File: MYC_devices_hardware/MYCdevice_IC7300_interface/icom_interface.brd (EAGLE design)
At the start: 83.8 x 32.7 mm, 42 parts, among them IC1 ATMEGA1284, IC2 MAX232, IC3 PCA9517, IC4 78L05, Q1 20MHz, Q2 BC817-40SMD, Q3 BC817-40SMD, Q4 BSS138, X1 8-15V, X2 1503_09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

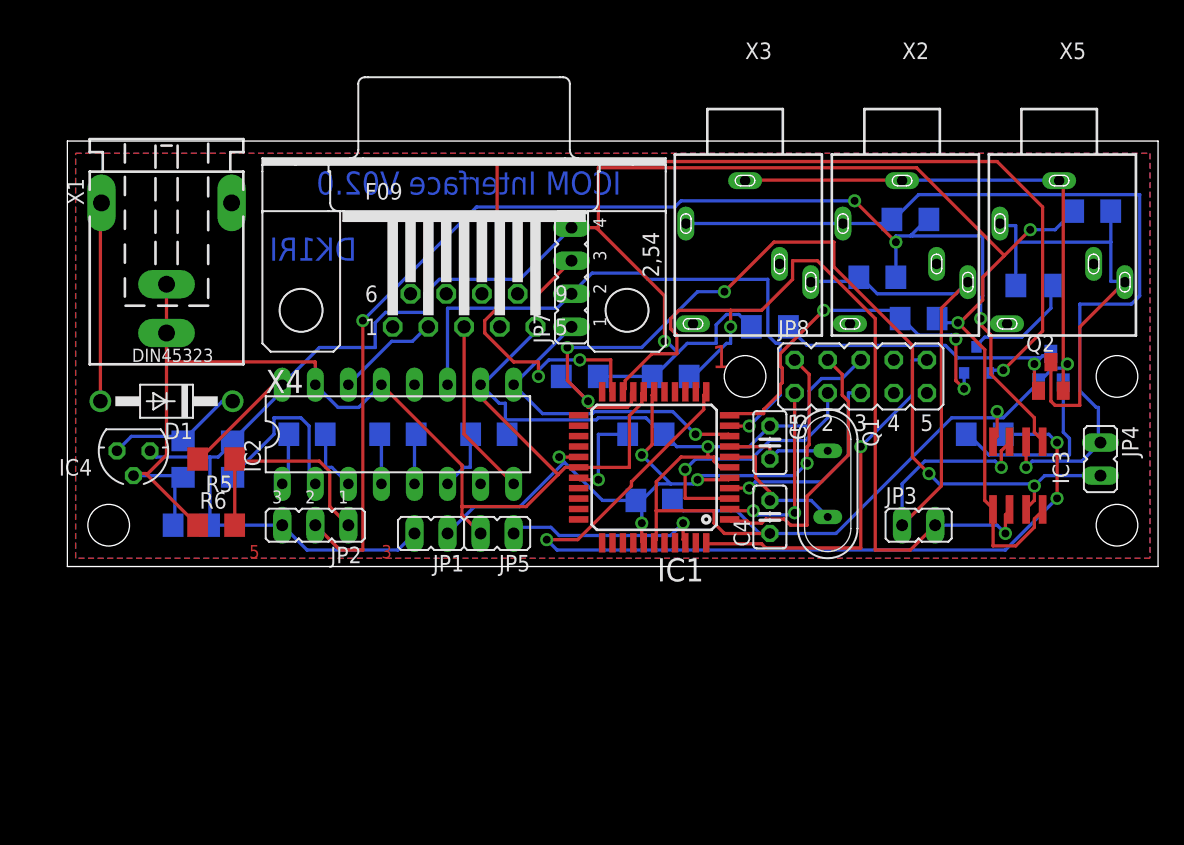
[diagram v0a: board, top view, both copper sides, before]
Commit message: wrong FET corrected, better layout
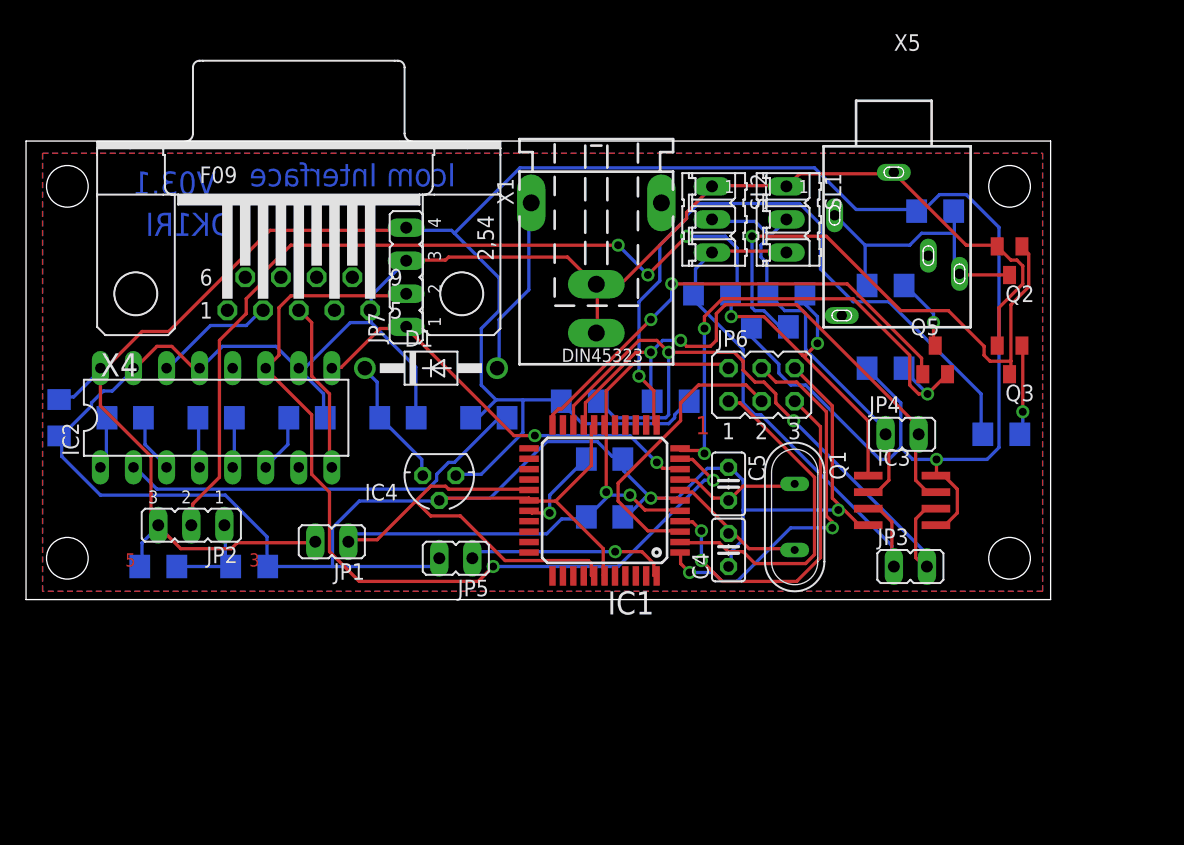
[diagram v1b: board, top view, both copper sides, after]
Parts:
- removed JP8: SPI/ISP, jumper:JP5Q
- removed Q4: BSS138, bss138_10:SOT23
- removed X2, X3: 1503_09, con-lumberg:1503_09
- added JP6: ISP, jumper:JP3Q
- added Q5: BSS84, transistor-small-signal:SOT23
- added SL1, SL2: I2C, con-amp-quick:03P
- C3: value 22uF 1210 -> 22uF
- R1, R2, R3, R4: value 10k -> see manual
- R10: value 100k -> 10k
- moved X1 33.0 mm to (43.8, 45.1)
- moved IC4 23.6 mm to (31.8, 24.1)
- moved D1 20.5 mm to (31.1, 32.4), turned to 0 degrees
- moved C8 19.9 mm to (35.6, 28.6), turned to 0 degrees
- moved C1 16.8 mm to (28.6, 28.6), turned to 180 degrees
- moved JP4 15.4 mm to (67.3, 27.3), turned to 270 degrees
- moved C9 14.0 mm to (21.6, 28.6)
- moved C6 14.0 mm to (7.62, 28.6)
- moved C7 14.0 mm to (14.6, 28.6)
- moved IC2 14.0 mm to (14.6, 28.6)
- moved C2 13.1 mm to (2.54, 28.6), turned to 270 degrees
- moved R1 12.8 mm to (52.7, 38.1)
- moved X4 12.8 mm to (21.0, 38.1)
- moved X5 12.7 mm to (66.7, 49.5)
- moved JP7 12.7 mm to (29.2, 39.4)
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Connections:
- removed net N$4: IC1.42, JP5.1
- net GND: now also JP6.6, SL1.1, SL2.1; no longer JP8.6, X2.1, X3.1
- net N$15: now also JP5.1; no longer JP8.10
- net N$18: now also JP6.5; no longer JP8.5
- net N$19: now also Q5.2; no longer Q4.2
- net N$20: now also JP6.3; no longer JP8.3
- net N$23: now also SL1.3, SL2.3; no longer X2.3, X3.3
- net N$25: now also SL1.2, SL2.2; no longer X2.2, X3.2
- net N$28: now also JP6.4; no longer JP8.4
- net N$29: now also Q5.3; no longer Q4.3
- net N$34: now also IC1.22, Q5.1; no longer IC1.21, Q4.1
- net N$6: now also JP6.1; no longer JP8.1
- net N$7: now also JP6.2; no longer JP8.2
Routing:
- net N$34: track 87.0 -> 37.6 mm, vias 3 -> 2
- net N$25: track 68.4 -> 32.7 mm, vias 1 -> 0
- net VDD: track 180.1 -> 213.8 mm, vias 3 -> 1
- net N$22: track 73.2 -> 45.9 mm, vias 5 -> 2
- net N$12: track 46.3 -> 68.3 mm, vias 1 -> 2
- net N$7: track 57.2 -> 78.5 mm, vias 5 -> 2
- net N$30: track 24.2 -> 43.8 mm
- net N$16: track 13.8 -> 31.9 mm
- net N$4: track 15.5 -> 0.00 mm, vias 1 -> 0
- net N$11: track 67.7 -> 52.5 mm, vias 3 -> 1
- net N$15: track 29.2 -> 15.7 mm
- net N$9: track 36.0 -> 22.6 mm
- net N$6: track 14.5 -> 26.3 mm, vias 2 -> 0
- net N$18: track 15.9 -> 27.6 mm, vias 1 -> 2
- net N$19: track 29.0 -> 39.6 mm
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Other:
- board size 83.8 x 32.7 mm -> 78.7 x 35.2 mm
- board text added: "Icom Interface"
- board text added: "V03.1"
- board text removed: "ICOM Interface V02.0"

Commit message: bascom added, and new board
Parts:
- moved Q3 14.6 mm to (75.6, 18.4)
- moved Q5 14.6 mm to (69.8, 18.4)
- moved R10 14.6 mm to (69.8, 29.8)
- moved R9 14.6 mm to (57.1, 21.0)
- moved X5 14.6 mm to (66.7, 34.9)
- moved C5 14.6 mm to (54.0, 8.89)
- moved IC1 14.6 mm to (44.5, 7.62)
- moved IC3 14.6 mm to (67.3, 7.62)
- moved JP1 14.6 mm to (23.5, 4.45)
- moved JP2 14.6 mm to (12.7, 5.71)
- moved JP3 14.6 mm to (67.9, 2.54)
- moved JP4 14.6 mm to (67.3, 12.7)
- moved JP5 14.6 mm to (33.0, 3.17)
- moved Q2 14.6 mm to (75.6, 26.0)
- moved R1 14.6 mm to (52.7, 23.5)
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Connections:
- net N$15: now also IC1.42; no longer IC1.44
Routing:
- net N$15: track 15.7 -> 14.1 mm
- removed copper zone on layer 1, net GND
- removed copper zone on layer 16, net GND
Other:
- board text added: "V03.2"
- board text removed: "V03.1"
